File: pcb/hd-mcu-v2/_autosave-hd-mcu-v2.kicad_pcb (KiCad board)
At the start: 2 copper layers, 70 x 116.4 mm, 31 parts

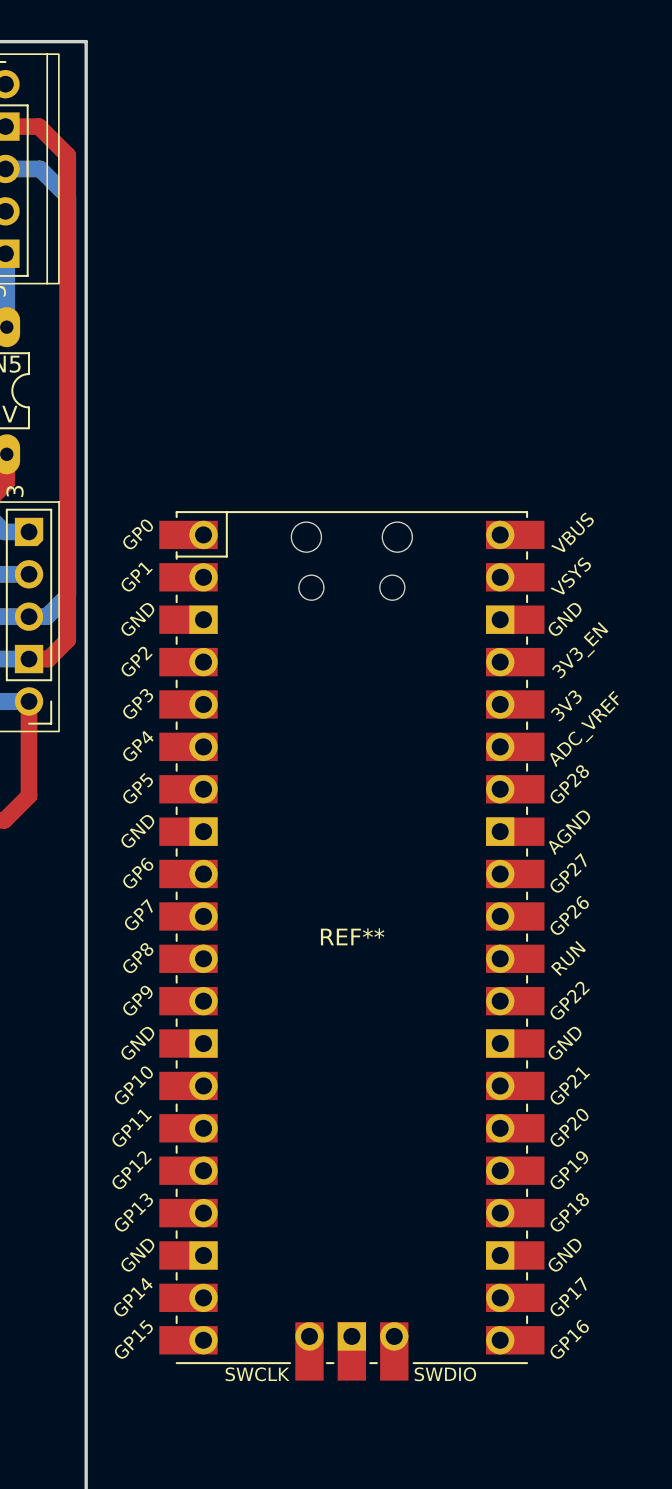
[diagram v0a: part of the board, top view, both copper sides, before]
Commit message: refactoring lifecycle
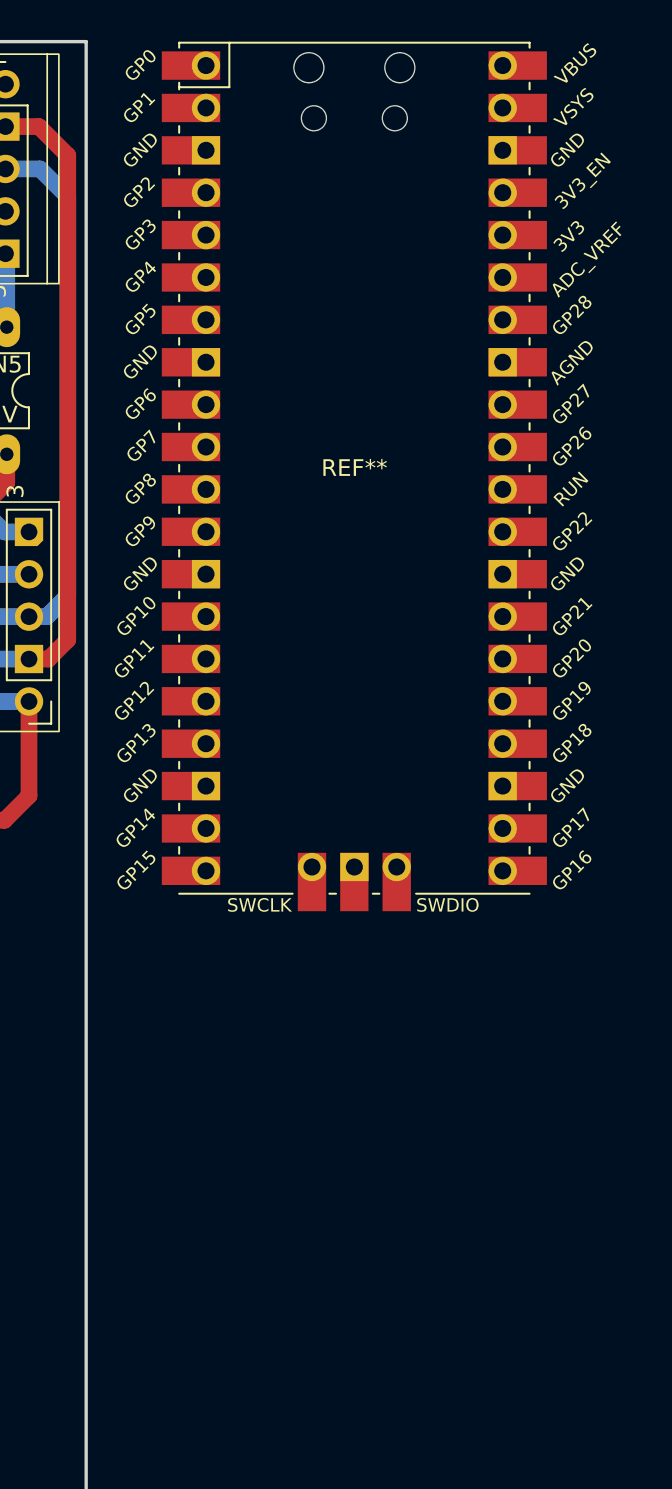
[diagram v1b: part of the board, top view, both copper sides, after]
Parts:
- moved REF** 28.1 mm to (110.7, 61.2)
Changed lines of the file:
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@@
   (net 37 "D_SPD")
   (footprint "denolk:RPi_Pico_SMD_TH" (layer "F.Cu")
-    (at 110.55 89.34)
+    (at 110.7 61.21)
     (descr "Through hole straight pin header, 2x20, 2.54mm pitch, double rows")
     (tags "Through hole pin header THT 2x20 2.54mm double row")
